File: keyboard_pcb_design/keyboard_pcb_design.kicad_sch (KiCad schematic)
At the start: 28 parts, among them J1 USB_C_Receptacle_USB2.0_14P, U1 SC09147, U2 NCP1117-3.3_SOT223, U3 MX25L3233FM2I-08Q, X1 ABM8-272-T3

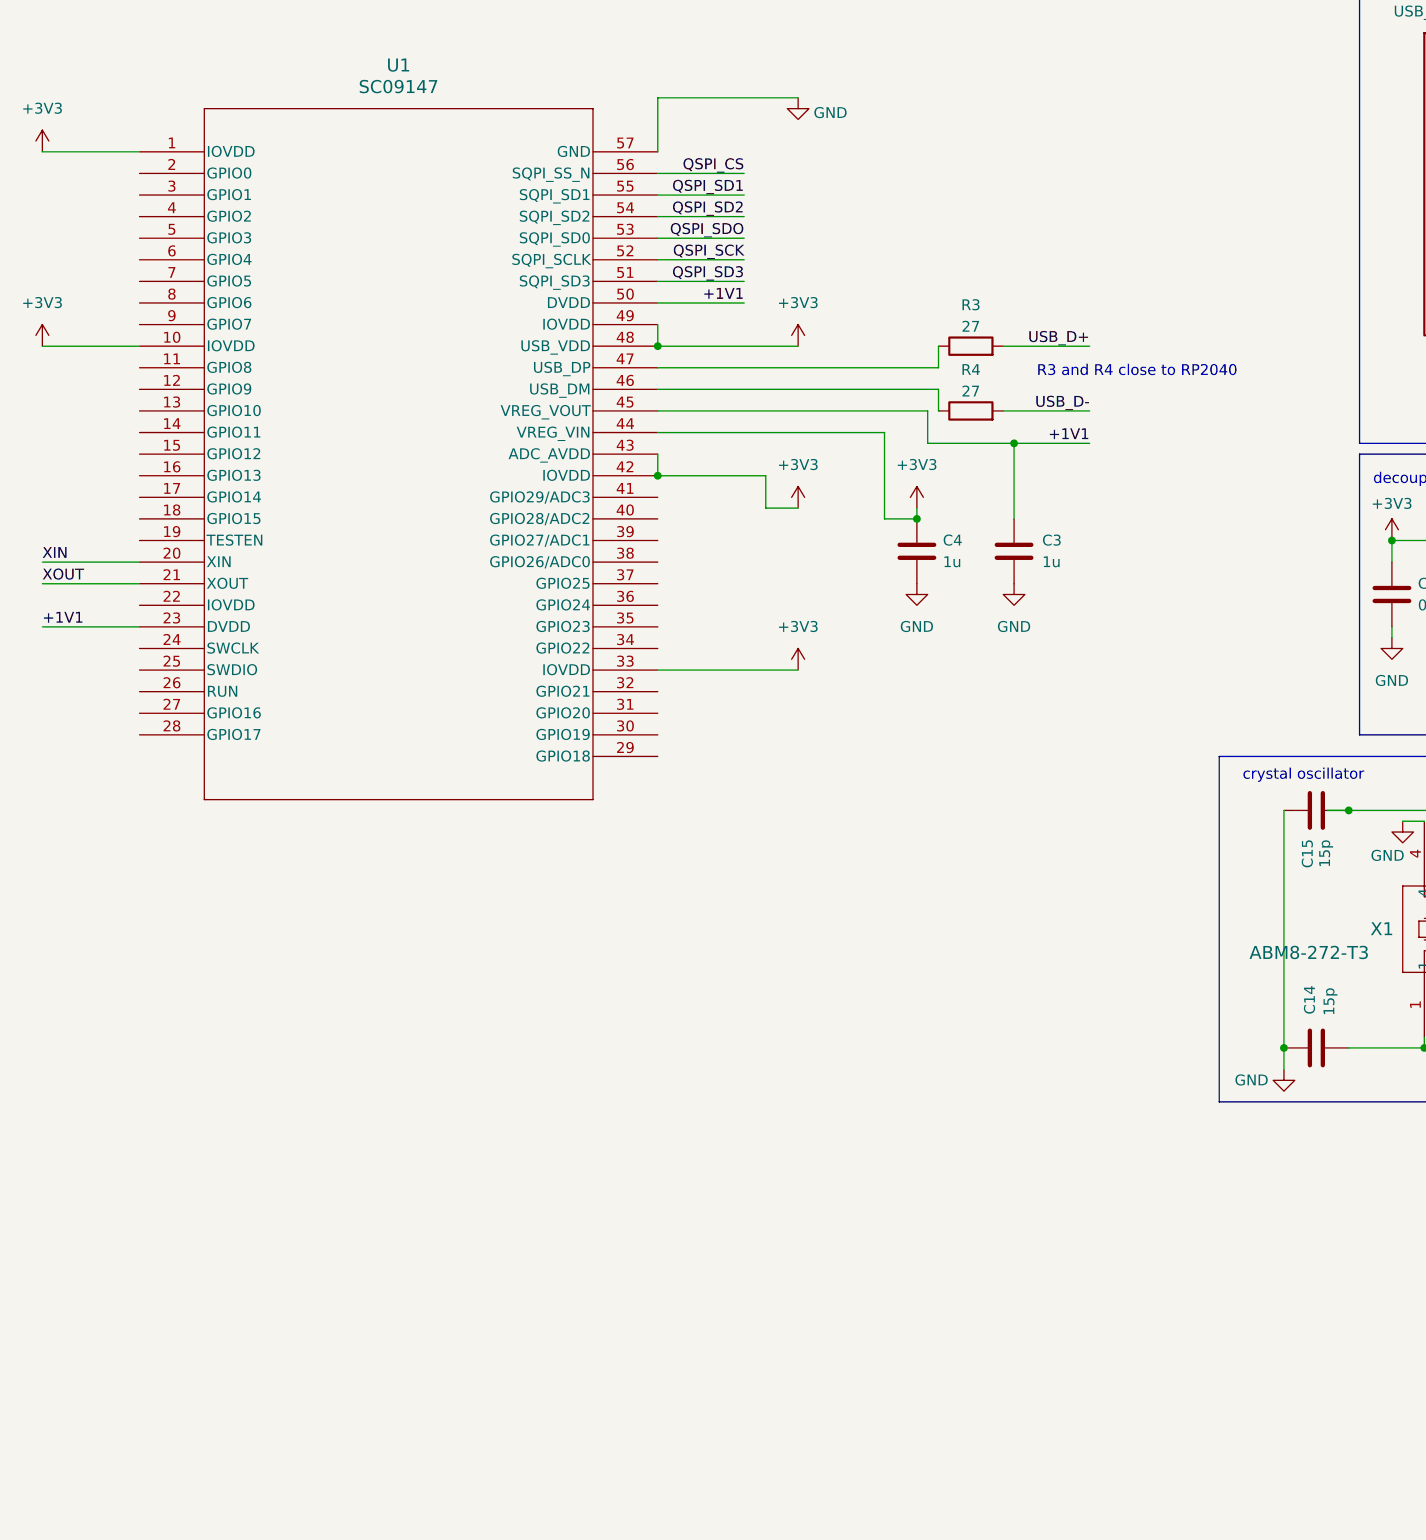
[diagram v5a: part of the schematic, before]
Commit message: key matrix schematic
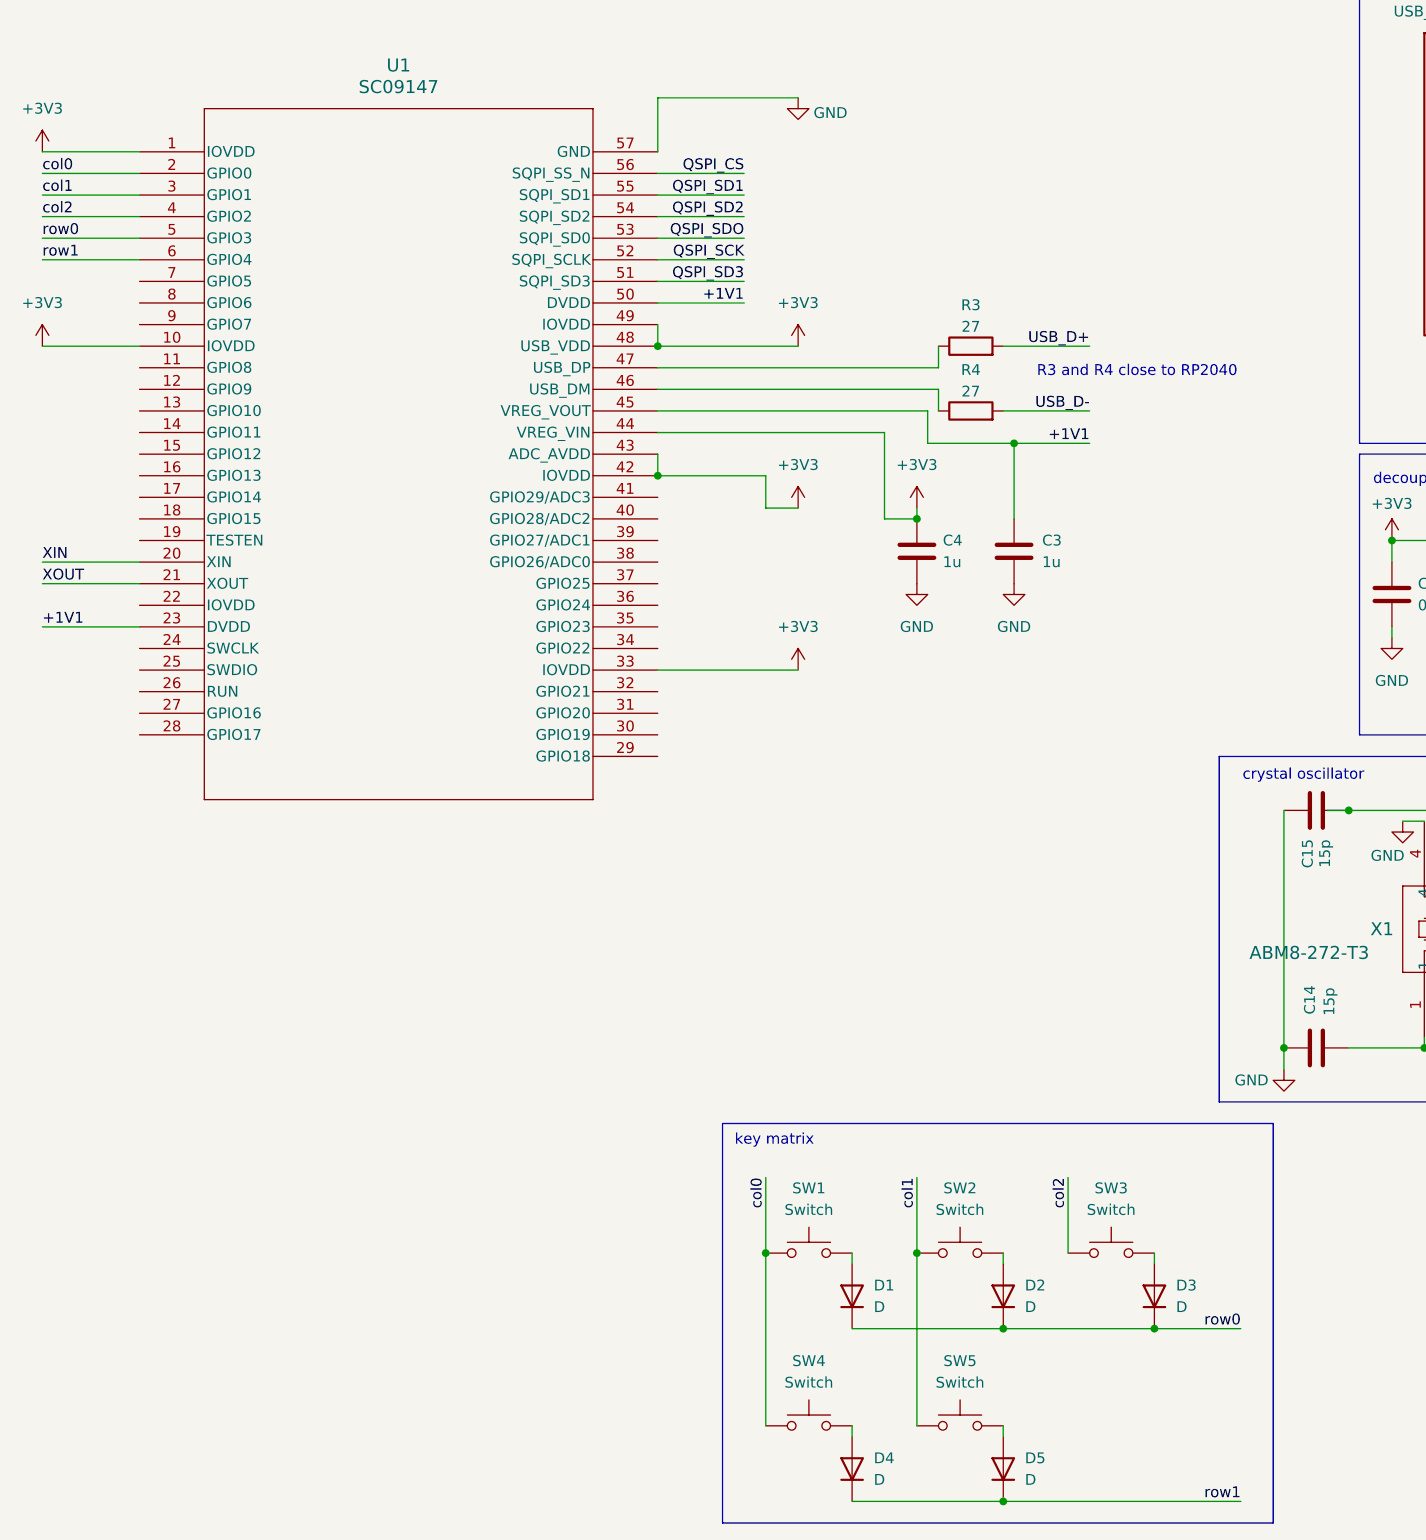
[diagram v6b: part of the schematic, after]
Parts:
- added D1, D3, D4, D5: D, Diode_SMD:D_0201_0603Metric, symbol Device:D
- added D2: D, symbol Device:D
- added SW1: Switch, Button_Switch_SMD:SW_SPST_TL3342, symbol tut_keyboard_library:Placeholder_Switch
- added SW2, SW3, SW4, SW5: Switch, symbol tut_keyboard_library:Placeholder_Switch
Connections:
- net col0: now reaches U1.2 (GPIO0)
- net col0: now also SW1.1, SW4.1
- net col1: now reaches U1.3 (GPIO1)
- net col1: now also SW2.1, SW5.1
- net col2: now reaches U1.4 (GPIO2)
- net col2: now also SW3.1
- net row0: now reaches U1.5 (GPIO3)
- net row0: now also D1.1 (K), D2.1 (K), D3.1 (K)
- net row1: now reaches U1.6 (GPIO4)
- net row1: now also D4.1 (K), D5.1 (K)
- new net: D1.2 (A), SW1.2
- new net: D3.2 (A), SW3.2
- new net: D2.2 (A), SW2.2
- new net: D4.2 (A), SW4.2
- new net: D5.2 (A), SW5.2
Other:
- note added: "key matrix"

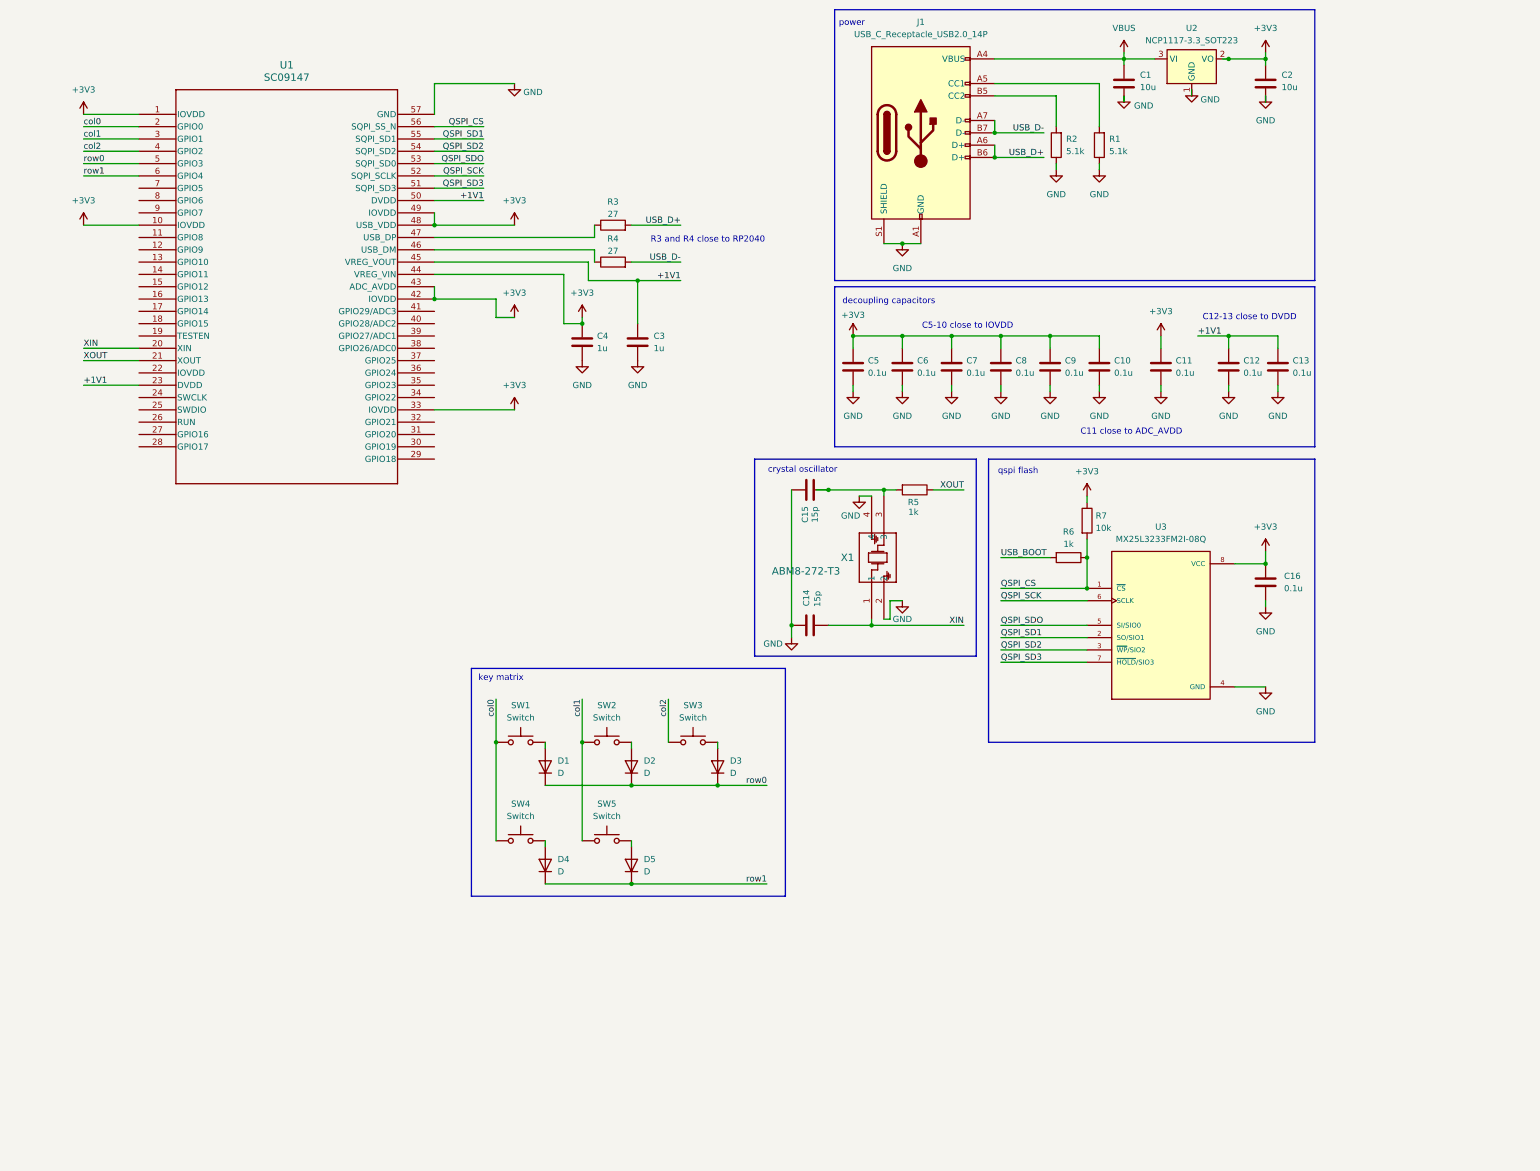
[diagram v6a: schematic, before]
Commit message: complete esd protection schematic
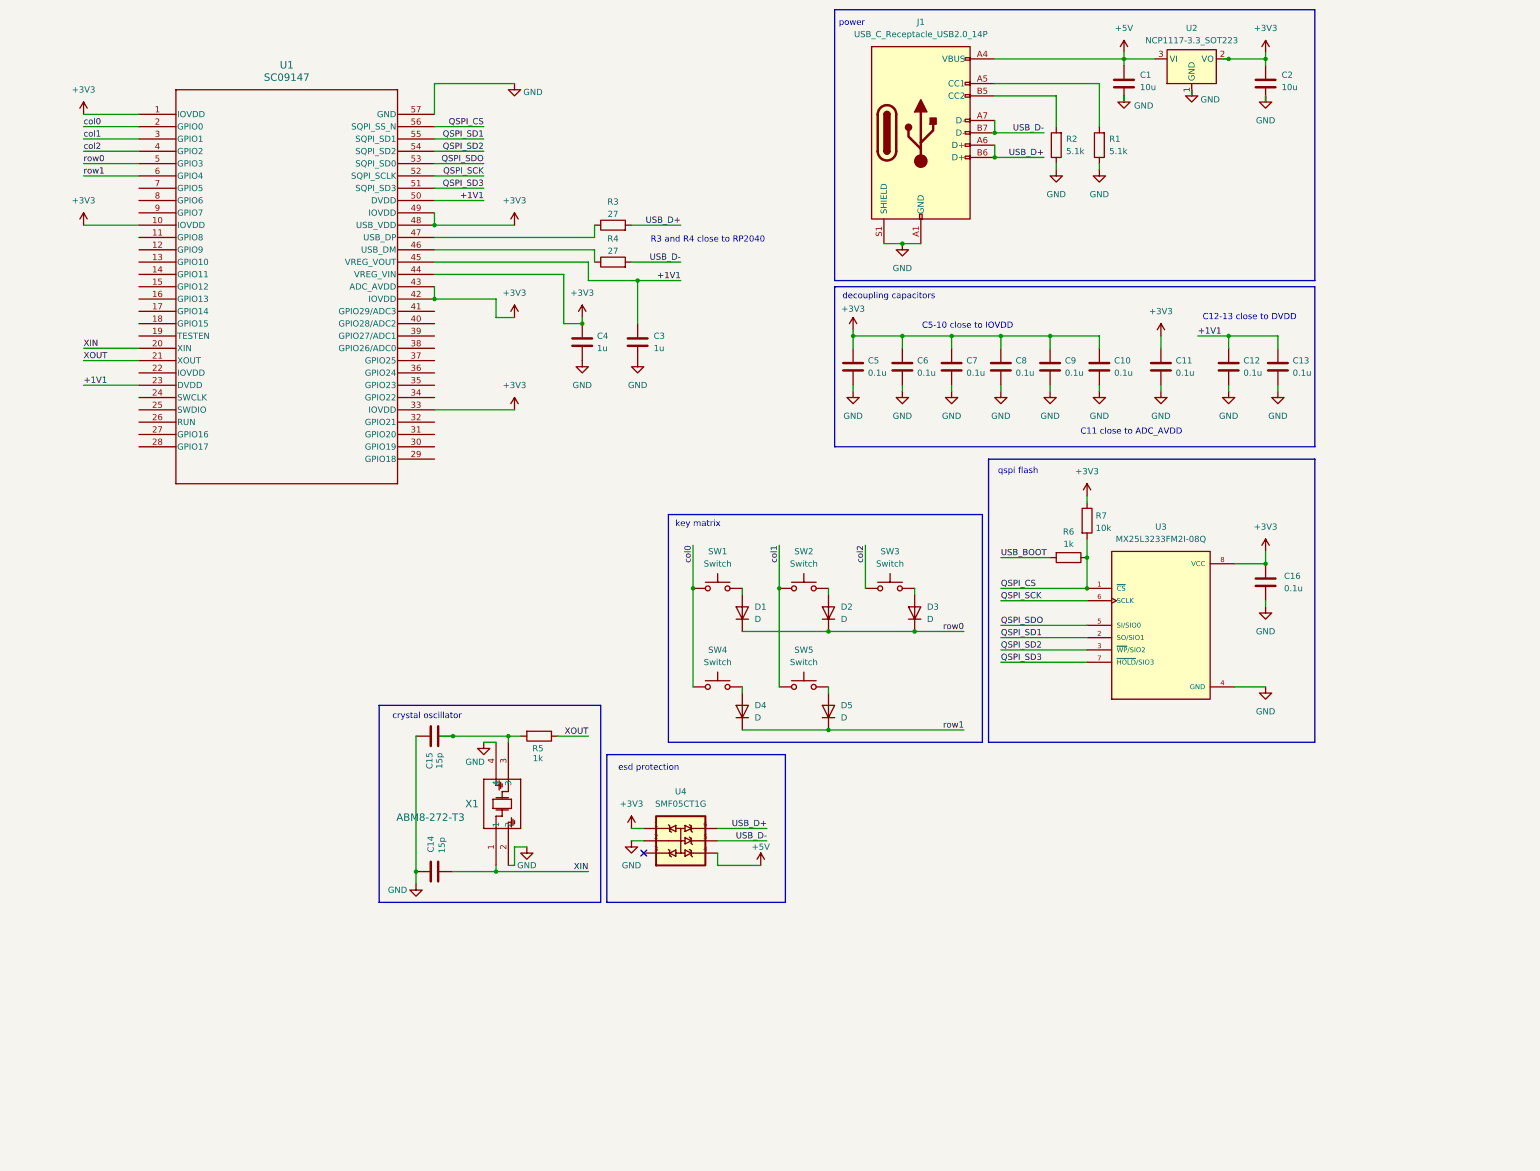
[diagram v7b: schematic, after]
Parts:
- added U4: SMF05CT1G, symbol keyboard_library:SMF05CT1G
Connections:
- net +3V3: now also U4.1
- net GND: now also U4.2
- net USB_D+: now also U4.6
- net USB_D-: now also U4.5
- net VBUS renamed +5V
- net +5V: now also U4.4
- no-connect marks 0 -> 1
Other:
- note added: "esd protection"
- moved on the sheet: C14, C15, D1, D2, D3, D4, D5, R5, SW1, SW2, SW3, SW4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
